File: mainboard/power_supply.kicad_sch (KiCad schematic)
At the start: 35 parts, among them J1 Conn_01x06

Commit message: Further work on the schematics/file organization
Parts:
- B1, B2, C1, C10, C12, C15, C5, C6, C8, C9, D10, D12: footprint ~ -> Package_DIP:DIP-14_W7.62mm
- B3: footprint ~ -> Package_DIP:DIP-16_W7.62mm
- CAP31, CAP32, CAP33, CAP34, CAP35, CAP36, CAP37: Comment (none) -> .3 LEAD SPACING
- REG1: Comment (none) -> ALT: LM7905
- REG3: Comment (none) -> ALT: LM7912
- REG4: Comment (none) -> ALT: LM7812
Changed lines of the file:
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@@
 			)
 		)
-		(property "Datasheet" ""
+		(property "Datasheet" "https://www.ti.com/lit/ds/symlink/lm79.pdf"
 			(at 139.7 26.67 0)
 			(hide yes)
@@
 			)
 		)
+		(property "Comment" "ALT: LM7905"
+			(at 144.78 33.02 0)
+			(hide yes)
+			(show_name no)
+			(do_not_autoplace no)
+			(effects
+				(font
+					(size 1.27 1.27)
+				)
+			)
+		)
 		(pin "1"
 		)
@@
 			)
 		)
-		(property "Datasheet" ""
+		(property "Datasheet" "https://www.ti.com/lit/ds/symlink/lm79.pdf"
 			(at 139.7 67.31 0)
 			(hide yes)
@@
 			)
 		)
+		(property "Comment" "ALT: LM7912"
+			(at 144.78 73.66 0)
+			(hide yes)
+			(show_name no)
+			(do_not_autoplace no)
+			(effects
+				(font
+					(size 1.27 1.27)
+				)
+			)
+		)
 		(pin "3"
 		)
@@
 			)
 		)
+		(property "Comment" "ALT: LM7812"
+			(at 144.78 93.98 0)
+			(hide yes)
+			(show_name no)
+			(do_not_autoplace no)
+			(effects
+				(font
+					(size 1.27 1.27)
+				)
+			)
+		)
 		(pin "2"
 		)
@@
 			)
 		)
+		(property "Comment" ".3 LEAD SPACING"
+			(at 124.46 77.47 0)
+			(hide yes)
+			(show_name no)
+			(do_not_autoplace no)
+			(effects
+				(font
+					(size 1.27 1.27)
+				)
+			)
+		)
 		(pin "1"
 		)
@@
 			)
 		)
+		(property "Comment" ".3 LEAD SPACING"
+			(at 170.18 77.47 0)
+			(hide yes)
+			(show_name no)
+			(do_not_autoplace no)
+			(effects
+				(font
+					(size 1.27 1.27)
+				)
+			)
+		)
 		(pin "1"
 		)
@@
 			)
 		)
+		(property "Comment" ".3 LEAD SPACING"
+			(at 170.18 57.15 0)
+			(hide yes)
+			(show_name no)
+			(do_not_autoplace no)
+			(effects
+				(font
+					(size 1.27 1.27)
+				)
+			)
+		)
 		(pin "2"
 		)
@@
 			)
 		)
+		(property "Comment" ".3 LEAD SPACING"
+			(at 170.18 36.83 0)
+			(hide yes)
+			(show_name no)
+			(do_not_autoplace no)
+			(effects
+				(font
+					(size 1.27 1.27)
+				)
+			)
+		)
 		(pin "2"
 		)
@@
 			)
 		)
+		(property "Comment" ".3 LEAD SPACING"
+			(at 124.46 97.79 0)
+			(hide yes)
+			(show_name no)
+			(do_not_autoplace no)
+			(effects
+				(font
+					(size 1.27 1.27)
+				)
+			)
+		)
 		(pin "2"
 		)
@@
 			)
 		)
+		(property "Comment" ".3 LEAD SPACING"
+			(at 170.18 97.79 0)
+			(hide yes)
+			(show_name no)
+			(do_not_autoplace no)
+			(effects
+				(font
+					(size 1.27 1.27)
+				)
+			)
+		)
 		(pin "2"
 		)
@@
 			)
 		)
+		(property "Comment" ".3 LEAD SPACING"
+			(at 124.46 57.15 0)
+			(hide yes)
+			(show_name no)
+			(do_not_autoplace no)
+			(effects
+				(font
+					(size 1.27 1.27)
+				)
+			)
+		)
 		(pin "1"
 		)
@@
 			)
 		)
-		(property "Footprint" "~"
+		(property "Footprint" "Package_DIP:DIP-14_W7.62mm"
 			(at 203.2 109.855 0)
 			(hide yes)
@@
 			)
 		)
-		(property "Datasheet" ""
+		(property "Datasheet" "https://www.ti.com/lit/ds/symlink/sn5450.pdf?ts=1779367727182"
 			(at 203.2 109.855 0)
 			(hide yes)
@@
 			)
 		)
-		(property "Description" ""
+		(property "Description" "DUAL 2-2-INPUT AND-OR-INVERT GATE"
 			(at 205.74 137.16 0)
 			(show_name no)
@@
 			)
 		)
-		(property "Footprint" "~"
+		(property "Footprint" "Package_DIP:DIP-14_W7.62mm"
 			(at 170.18 137.16 0)
 			(hide yes)
@@
 			)
 		)
-		(property "Datasheet" "~"
+		(property "Datasheet" "https://www.futurlec.com/74/IC7404.shtml"
 			(at 170.18 137.16 0)
 			(hide yes)
@@
 			)
 		)
-		(property "Description" ""
+		(property "Description" "HEX INVERTER"
 			(at 170.18 137.16 0)
 			(show_name no)
@@
 			)
 		)
-		(property "Footprint" "~"
+		(property "Footprint" "Package_DIP:DIP-14_W7.62mm"
 			(at 223.52 137.16 0)
 			(hide yes)
@@
 			)
 		)
-		(property "Datasheet" "~"
+		(property "Datasheet" "https://www.futurlec.com/74/IC7427.shtml"
 			(at 223.52 137.16 0)
 			(hide yes)
@@
 			)
 		)
-		(property "Description" ""
+		(property "Description" "TRIPLE 3-INPUT NOR GATE"
 			(at 223.52 137.16 0)
 			(show_name no)
@@
 			)
 		)
-		(property "Footprint" "~"
+		(property "Footprint" "Package_DIP:DIP-14_W7.62mm"
 			(at 121.92 137.16 0)
 			(hide yes)
@@
 			)
 		)
-		(property "Datasheet" "~"
+		(property "Datasheet" "https://www.futurlec.com/74/IC7410.shtml"
 			(at 121.92 137.16 0)
 			(hide yes)
@@
 			)
 		)
-		(property "Description" ""
+		(property "Description" "TRIPLE 3-INPUT NAND GATE"
 			(at 121.92 137.16 0)
 			(show_name no)
@@
 			)
 		)
-		(property "Footprint" "~"
+		(property "Footprint" "Package_DIP:DIP-14_W7.62mm"
 			(at 241.3 137.16 0)
 			(hide yes)
@@
 			)
 		)
-		(property "Datasheet" "~"
+		(property "Datasheet" "https://www.futurlec.com/74/IC7432.shtml"
 			(at 241.3 137.16 0)
 			(hide yes)
@@
 			)
 		)
-		(property "Description" ""
+		(property "Description" "QUAD 2-INPUT OR GATE"
 			(at 241.3 137.16 0)
 			(show_name no)
@@
 			)
 		)
-		(property "Footprint" "~"
+		(property "Footprint" "Package_DIP:DIP-14_W7.62mm"
 			(at 187.96 137.16 0)
 			(hide yes)
@@
 			)
 		)
-		(property "Datasheet" "~"
+		(property "Datasheet" "https://www.futurlec.com/74/IC7402.shtml"
 			(at 187.96 137.16 0)
 			(hide yes)
@@
 			)
 		)
-		(property "Description" ""
+		(property "Description" "QUAD 2-INPUT NOR GATE"
 			(at 187.96 137.16 0)
 			(show_name no)
@@
 			)
 		)
-		(property "Footprint" "~"
+		(property "Footprint" "Package_DIP:DIP-14_W7.62mm"
 			(at 259.08 137.16 0)
 			(hide yes)
@@
 			)
 		)
-		(property "Datasheet" "~"
+		(property "Datasheet" "https://www.ti.com/lit/ds/symlink/sn74ls08.pdf?ts=1779367913652&ref_url=https%253A%252F%252Fwww.ti.com%252Fproduct%252FSN74LS08%253Futm_source%253Dgoogle%2526utm_medium%253Dcpc%2526utm_campaign%253Dasc-int-null-44700045336317929_prodfolderdynamic-cpc-pf-google-ww_en_int%2526utm_content%253Dprodfolddynamic%2526ds_k%253DDYNAMIC+SEARCH+ADS%2526DCM%253Dyes%2526gclsrc%253Daw.ds%2526gad_source%253D1%2526gad_campaignid%253D12514844049%2526gclid%253DCjwKCAjw2rrQBhBuEiwAarLWHWx_QNQbALFt2IgWJV-S5n-LY28ZOQM9yUHhG5f6aODST_t2Ov5OGxoCKG4QAvD_BwE"
 			(at 259.08 137.16 0)
 			(hide yes)
@@
 			)
 		)
-		(property "Description" ""
+		(property "Description" "QUAD 2-INPUT AND GATE"
 			(at 259.08 137.16 0)
 			(show_name no)
@@
 			)
 		)
-		(property "Datasheet" ""
+		(property "Datasheet" "https://datasheet4u.com/pdf/513466/DM8097.pdf"
 			(at 33.02 125.095 0)
 			(hide yes)
@@
 			)
 		)
-		(property "Datasheet" ""
+		(property "Datasheet" "https://datasheet4u.com/pdf/513466/DM8097.pdf"
 			(at 45.72 125.095 0)
 			(hide yes)
@@
 			)
 		)
-		(property "Footprint" "~"
+		(property "Footprint" "Package_DIP:DIP-14_W7.62mm"
 			(at 66.04 137.16 0)
 			(hide yes)
@@
 			)
 		)
-		(property "Datasheet" "~"
+		(property "Datasheet" "https://www.futurlec.com/74/IC7400.shtml"
 			(at 66.04 137.16 0)
 			(hide yes)
@@
 			)
 		)
-		(property "Description" ""
+		(property "Description" "QUAD 2-INPUT NAND GATE"
 			(at 66.04 137.16 0)
 			(show_name no)
@@
 			)
 		)
-		(property "Footprint" "~"
+		(property "Footprint" "Package_DIP:DIP-14_W7.62mm"
 			(at 78.74 137.16 0)
 			(hide yes)
@@
 			)
 		)
-		(property "Datasheet" "~"
+		(property "Datasheet" "https://www.futurlec.com/74/IC7400.shtml"
 			(at 78.74 137.16 0)
 			(hide yes)
@@
 			)
 		)
-		(property "Description" ""
+		(property "Description" "QUAD 2-INPUT NAND GATE"
 			(at 78.74 137.16 0)
 			(show_name no)
@@
 			)
 		)
-		(property "Footprint" "~"
+		(property "Footprint" "Package_DIP:DIP-14_W7.62mm"
 			(at 91.44 137.16 0)
 			(hide yes)
@@
 			)
 		)
-		(property "Datasheet" "~"
+		(property "Datasheet" "https://www.futurlec.com/74/IC7400.shtml"
 			(at 91.44 137.16 0)
 			(hide yes)
@@
 			)
 		)
-		(property "Description" ""
+		(property "Description" "QUAD 2-INPUT NAND GATE"
 			(at 91.44 137.16 0)
 			(show_name no)
@@
 			)
 		)
-		(property "Footprint" "~"
+		(property "Footprint" "Package_DIP:DIP-14_W7.62mm"
 			(at 109.22 137.16 0)
 			(hide yes)
@@
 			)
 		)
-		(property "Datasheet" "~"
+		(property "Datasheet" "https://www.futurlec.com/74/IC7410.shtml"
 			(at 109.22 137.16 0)
 			(hide yes)
@@
 			)
 		)
-		(property "Description" ""
+		(property "Description" "TRIPLE 3-INPUT NAND GATE"
 			(at 109.22 137.16 0)
 			(show_name no)
@@
 			)
 		)
-		(property "Footprint" "~"
+		(property "Footprint" "Package_DIP:DIP-16_W7.62mm"
 			(at 139.7 137.16 0)
 			(hide yes)
@@
 			)
 		)
-		(property "Datasheet" "~"
+		(property "Datasheet" "https://www.ti.com/lit/ds/symlink/sn74123.pdf?ts=1779367555065&ref_url=https%253A%252F%252Fwww.ti.com%252Fproduct%252FSN74123"
 			(at 139.7 137.16 0)
 			(hide yes)
@@
 			)
 		)
-		(property "Description" ""
+		(property "Description" "MULTIVIBRATOR"
 			(at 139.7 137.16 0)
 			(show_name no)
@@
 			)
 		)
-		(property "Footprint" "~"
+		(property "Footprint" "Package_DIP:DIP-14_W7.62mm"
 			(at 157.48 137.16 0)
 			(hide yes)
@@
 			)
 		)
-		(property "Datasheet" "~"
+		(property "Datasheet" "https://www.futurlec.com/74/IC7404.shtml"
 			(at 157.48 137.16 0)
 			(hide yes)
@@
 			)
 		)
-		(property "Description" ""
+		(property "Description" "HEX INVERTER"
 			(at 157.48 137.16 0)
 			(show_name no)

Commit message: Additional  work on mainboard
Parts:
- A10, A9: footprint ~ -> Package_DIP:DIP-16_W7.62mm
- CAP31, DI5, DI6, DI7, DI8, REG1, REG2, REG3, REG4: footprint ~ -> (none)
- CAP32, CAP33: footprint ~ -> Capacitor_THT:CP_Axial_L55.0mm_D26.0mm_P60.00mm_Horizontal
- CAP34, CAP35, CAP36, CAP37: footprint ~ -> Capacitor_THT:C_Axial_L12.0mm_D6.5mm_P20.00mm_Horizontal
- J1: footprint ~ -> Connector_JST:JST_VH_B6P-VH_1x06_P3.96mm_Vertical
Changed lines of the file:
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@@
 			)
 		)
-		(property "Footprint" "~"
+		(property "Footprint" ""
 			(at 139.7 26.67 0)
 			(hide yes)
@@
 			)
 		)
-		(property "Footprint" "~"
+		(property "Footprint" ""
 			(at 139.7 67.31 0)
 			(hide yes)
@@
 			)
 		)
-		(property "Footprint" "~"
+		(property "Footprint" ""
 			(at 140.97 46.99 0)
 			(hide yes)
@@
 			)
 		)
-		(property "Footprint" "~"
+		(property "Footprint" ""
 			(at 146.05 86.36 0)
 			(hide yes)
@@
 			)
 		)
-		(property "Footprint" "~"
+		(property "Footprint" "Capacitor_THT:CP_Axial_L55.0mm_D26.0mm_P60.00mm_Horizontal"
 			(at 124.46 77.47 0)
 			(hide yes)
@@
 			)
 		)
-		(property "Datasheet" "~"
+		(property "Datasheet" ""
 			(at 124.46 77.47 0)
 			(hide yes)
@@
 			)
 		)
-		(property "Footprint" "~"
+		(property "Footprint" "Capacitor_THT:C_Axial_L12.0mm_D6.5mm_P20.00mm_Horizontal"
 			(at 170.18 77.47 0)
 			(hide yes)
@@
 			)
 		)
-		(property "Datasheet" "~"
+		(property "Datasheet" ""
 			(at 170.18 77.47 0)
 			(hide yes)
@@
 			)
 		)
-		(property "Footprint" "~"
+		(property "Footprint" "Capacitor_THT:C_Axial_L12.0mm_D6.5mm_P20.00mm_Horizontal"
 			(at 170.18 57.15 0)
 			(hide yes)
@@
 			)
 		)
-		(property "Datasheet" "~"
+		(property "Datasheet" ""
 			(at 170.18 57.15 0)
 			(hide yes)
@@
 			)
 		)
-		(property "Footprint" "~"
+		(property "Footprint" "Capacitor_THT:C_Axial_L12.0mm_D6.5mm_P20.00mm_Horizontal"
 			(at 170.18 36.83 0)
 			(hide yes)
@@
 			)
 		)
-		(property "Datasheet" "~"
+		(property "Datasheet" ""
 			(at 170.18 36.83 0)
 			(hide yes)
@@
 			)
 		)
-		(property "Footprint" "~"
+		(property "Footprint" "Capacitor_THT:CP_Axial_L55.0mm_D26.0mm_P60.00mm_Horizontal"
 			(at 124.46 97.79 0)
 			(hide yes)
@@
 			)
 		)
-		(property "Footprint" "~"
+		(property "Footprint" "Capacitor_THT:C_Axial_L12.0mm_D6.5mm_P20.00mm_Horizontal"
 			(at 170.18 97.79 0)
 			(hide yes)
@@
 			)
 		)
-		(property "Datasheet" "~"
+		(property "Datasheet" ""
 			(at 170.18 97.79 0)
 			(hide yes)
@@
 			)
 		)
-		(property "Footprint" "~"
+		(property "Footprint" ""
 			(at 97.79 68.58 0)
 			(hide yes)
@@
 			)
 		)
-		(property "Footprint" "~"
+		(property "Footprint" ""
 			(at 97.79 73.66 0)
 			(hide yes)
@@
 			)
 		)
-		(property "Footprint" "~"
+		(property "Footprint" ""
 			(at 97.79 78.74 0)
 			(hide yes)
@@
 			)
 		)
-		(property "Footprint" "~"
+		(property "Footprint" ""
 			(at 97.79 83.82 0)
 			(hide yes)
@@
 			)
 		)
-		(property "Footprint" "~"
+		(property "Footprint" ""
 			(at 124.46 57.15 0)
 			(hide yes)
@@
 			)
 		)
-		(property "Footprint" "~"
+		(property "Footprint" "Connector_JST:JST_VH_B6P-VH_1x06_P3.96mm_Vertical"
 			(at 58.42 55.88 0)
 			(hide yes)
@@
 			)
 		)
-		(property "Datasheet" "~"
+		(property "Datasheet" "https://www.jst-mfg.com/product/pdf/eng/eVH.pdf"
 			(at 58.42 55.88 0)
 			(hide yes)
@@
 			)
 		)
-		(property "Footprint" "~"
+		(property "Footprint" "Package_DIP:DIP-16_W7.62mm"
 			(at 33.02 125.095 0)
 			(hide yes)
@@
 			)
 		)
-		(property "Description" ""
+		(property "Description" "TRI-STATE HEX BUFFER"
 			(at 35.56 137.16 0)
 			(show_name no)
@@
 			)
 		)
-		(property "Footprint" "~"
+		(property "Footprint" "Package_DIP:DIP-16_W7.62mm"
 			(at 45.72 125.095 0)
 			(hide yes)
@@
 			)
 		)
-		(property "Description" ""
+		(property "Description" "TRI-STATE HEX BUFFER"
 			(at 48.26 137.16 0)
 			(show_name no)

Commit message: Progress 20260526
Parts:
- DI5, DI6, DI7, DI8: footprint (none) -> Diode_THT:D_DO-41_SOD81_P10.16mm_Horizontal
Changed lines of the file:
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@@
 			)
 		)
-		(property "Footprint" ""
+		(property "Footprint" "Diode_THT:D_DO-41_SOD81_P10.16mm_Horizontal"
 			(at 97.79 68.58 0)
 			(hide yes)
@@
 			)
 		)
-		(property "Footprint" ""
+		(property "Footprint" "Diode_THT:D_DO-41_SOD81_P10.16mm_Horizontal"
 			(at 97.79 73.66 0)
 			(hide yes)
@@
 			)
 		)
-		(property "Footprint" ""
+		(property "Footprint" "Diode_THT:D_DO-41_SOD81_P10.16mm_Horizontal"
 			(at 97.79 78.74 0)
 			(hide yes)
@@
 			)
 		)
-		(property "Footprint" ""
+		(property "Footprint" "Diode_THT:D_DO-41_SOD81_P10.16mm_Horizontal"
 			(at 97.79 83.82 0)
 			(hide yes)

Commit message: Additional  work on mainboard
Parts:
- A10, A9, B3: footprint Package_DIP:DIP-16_W7.62mm -> mainboard:apple-1_DIP-16_W7.62mm
- B1, B2, C1, C10, C12, C15, C5, C6, C8, C9, D10, D12: footprint Package_DIP:DIP-14_W7.62mm -> mainboard:apple-1_DIP-14_W7.62mm
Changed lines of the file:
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@@
 			)
 		)
-		(property "Footprint" "Package_DIP:DIP-14_W7.62mm"
+		(property "Footprint" "mainboard:apple-1_DIP-14_W7.62mm"
 			(at 203.2 109.855 0)
 			(hide yes)
@@
 			)
 		)
-		(property "Footprint" "Package_DIP:DIP-14_W7.62mm"
+		(property "Footprint" "mainboard:apple-1_DIP-14_W7.62mm"
 			(at 170.18 137.16 0)
 			(hide yes)
@@
 			)
 		)
-		(property "Footprint" "Package_DIP:DIP-14_W7.62mm"
+		(property "Footprint" "mainboard:apple-1_DIP-14_W7.62mm"
 			(at 223.52 137.16 0)
 			(hide yes)
@@
 			)
 		)
-		(property "Footprint" "Package_DIP:DIP-14_W7.62mm"
+		(property "Footprint" "mainboard:apple-1_DIP-14_W7.62mm"
 			(at 121.92 137.16 0)
 			(hide yes)
@@
 			)
 		)
-		(property "Footprint" "Package_DIP:DIP-14_W7.62mm"
+		(property "Footprint" "mainboard:apple-1_DIP-14_W7.62mm"
 			(at 241.3 137.16 0)
 			(hide yes)
@@
 			)
 		)
-		(property "Footprint" "Package_DIP:DIP-14_W7.62mm"
+		(property "Footprint" "mainboard:apple-1_DIP-14_W7.62mm"
 			(at 187.96 137.16 0)
 			(hide yes)
@@
 			)
 		)
-		(property "Footprint" "Package_DIP:DIP-14_W7.62mm"
+		(property "Footprint" "mainboard:apple-1_DIP-14_W7.62mm"
 			(at 259.08 137.16 0)
 			(hide yes)
@@
 			)
 		)
-		(property "Footprint" "Package_DIP:DIP-16_W7.62mm"
+		(property "Footprint" "mainboard:apple-1_DIP-16_W7.62mm"
 			(at 33.02 125.095 0)
 			(hide yes)
@@
 			)
 		)
-		(property "Footprint" "Package_DIP:DIP-16_W7.62mm"
+		(property "Footprint" "mainboard:apple-1_DIP-16_W7.62mm"
 			(at 45.72 125.095 0)
 			(hide yes)
@@
 			)
 		)
-		(property "Footprint" "Package_DIP:DIP-14_W7.62mm"
+		(property "Footprint" "mainboard:apple-1_DIP-14_W7.62mm"
 			(at 66.04 137.16 0)
 			(hide yes)
@@
 			)
 		)
-		(property "Footprint" "Package_DIP:DIP-14_W7.62mm"
+		(property "Footprint" "mainboard:apple-1_DIP-14_W7.62mm"
 			(at 78.74 137.16 0)
 			(hide yes)
@@
 			)
 		)
-		(property "Footprint" "Package_DIP:DIP-14_W7.62mm"
+		(property "Footprint" "mainboard:apple-1_DIP-14_W7.62mm"
 			(at 91.44 137.16 0)
 			(hide yes)
@@
 			)
 		)
-		(property "Footprint" "Package_DIP:DIP-14_W7.62mm"
+		(property "Footprint" "mainboard:apple-1_DIP-14_W7.62mm"
 			(at 109.22 137.16 0)
 			(hide yes)
@@
 			)
 		)
-		(property "Footprint" "Package_DIP:DIP-16_W7.62mm"
+		(property "Footprint" "mainboard:apple-1_DIP-16_W7.62mm"
 			(at 139.7 137.16 0)
 			(hide yes)
@@
 			)
 		)
-		(property "Footprint" "Package_DIP:DIP-14_W7.62mm"
+		(property "Footprint" "mainboard:apple-1_DIP-14_W7.62mm"
 			(at 157.48 137.16 0)
 			(hide yes)

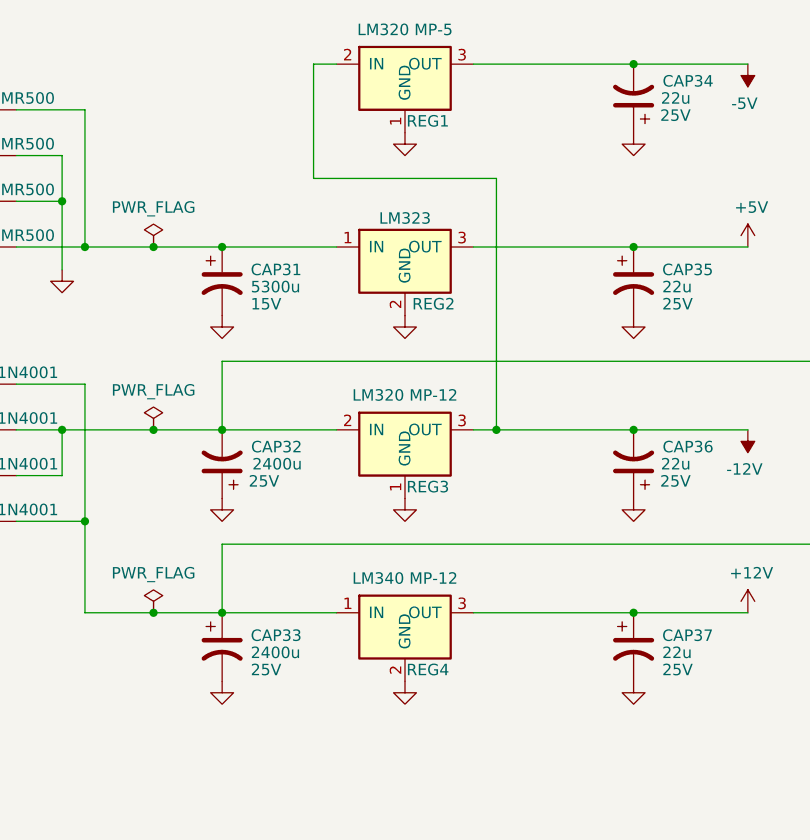
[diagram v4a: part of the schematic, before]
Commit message: large renaming, tidying up files, old libraries
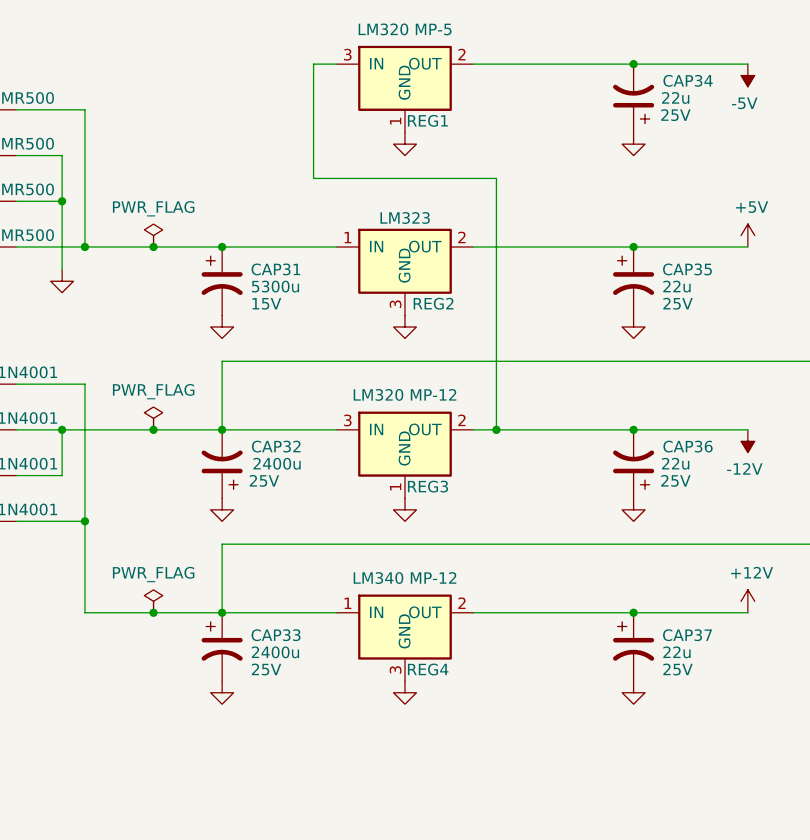
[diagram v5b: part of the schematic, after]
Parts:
- REG1, REG3, REG4: footprint (none) -> Package_TO_SOT_THT:TO-220-3_Vertical
- REG2: footprint (none) -> mainboard:TO-3
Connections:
- net +12V: now also REG4.2 (OUT); no longer REG4.3 (OUT)
- net +5V: now also REG2.2 (OUT); no longer REG2.3 (OUT)
- net -12V: now also REG1.3 (IN), REG3.2 (OUT); no longer REG1.2 (IN), REG3.3 (OUT)
- net -12V_UNREG: now also REG3.3 (IN); no longer REG3.2 (IN)
- net -5V: now also REG1.2 (OUT); no longer REG1.3 (OUT)
- net GND: now also REG2.3 (GND), REG4.3 (GND); no longer REG2.2 (GND), REG4.2 (GND)
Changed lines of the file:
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@@
 	)
 	(symbol
+		(lib_name "LM320_TO220_1")
 		(lib_id "apple1:LM320_TO220")
 		(at 144.78 33.02 0)
@@
 			)
 		)
-		(property "Footprint" ""
+		(property "Footprint" "Package_TO_SOT_THT:TO-220-3_Vertical"
 			(at 139.7 26.67 0)
 			(hide yes)
@@
 			)
 		)
-		(property "Description" ""
+		(property "Description" "3-Terminal Negative Regulator"
 			(at 144.78 33.02 0)
+			(hide yes)
 			(show_name no)
 			(do_not_autoplace no)
@@
 			)
 		)
-		(property "Footprint" ""
+		(property "Footprint" "Package_TO_SOT_THT:TO-220-3_Vertical"
 			(at 139.7 67.31 0)
 			(hide yes)
@@
 			)
 		)
-		(property "Description" ""
+		(property "Description" "3-Terminal Negative Regulator"
 			(at 144.78 73.66 0)
+			(hide yes)
 			(show_name no)
 			(do_not_autoplace no)
@@
 			)
 		)
-		(property "Footprint" ""
+		(property "Footprint" "mainboard:TO-3"
 			(at 140.97 46.99 0)
 			(hide yes)
@@
 			)
 		)
-		(property "Description" ""
+		(property "Description" "5-Volt Positive Regulator"
 			(at 144.78 53.34 0)
+			(hide yes)
 			(show_name no)
 			(do_not_autoplace no)
@@
 			)
 		)
-		(property "Footprint" ""
+		(property "Footprint" "Package_TO_SOT_THT:TO-220-3_Vertical"
 			(at 146.05 86.36 0)
 			(hide yes)
@@
 			)
 		)
-		(property "Description" ""
+		(property "Description" "1.5A Fixed Voltage Regulators"
 			(at 144.78 93.98 0)
-			(show_name no)
-			(do_not_autoplace no)
+			(hide yes)
+			(show_name no)
+			(do_not_autoplace no)

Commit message: 20260605
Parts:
- CAP32, CAP33: footprint Capacitor_THT:CP_Axial_L55.0mm_D26.0mm_P60.00mm_Horizontal -> mainboard:apple-1_CP_Axial_L55.0mm_D26.0mm_P55.88mm_Horizontal
